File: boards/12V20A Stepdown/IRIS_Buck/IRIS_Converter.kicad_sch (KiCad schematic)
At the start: 27 parts, among them J1 TB005-762-02BE, J2 TB005-762-02BE, Q1 CSD17571Q2, Q2 CSD16340Q3, U1 LM25145RGYR

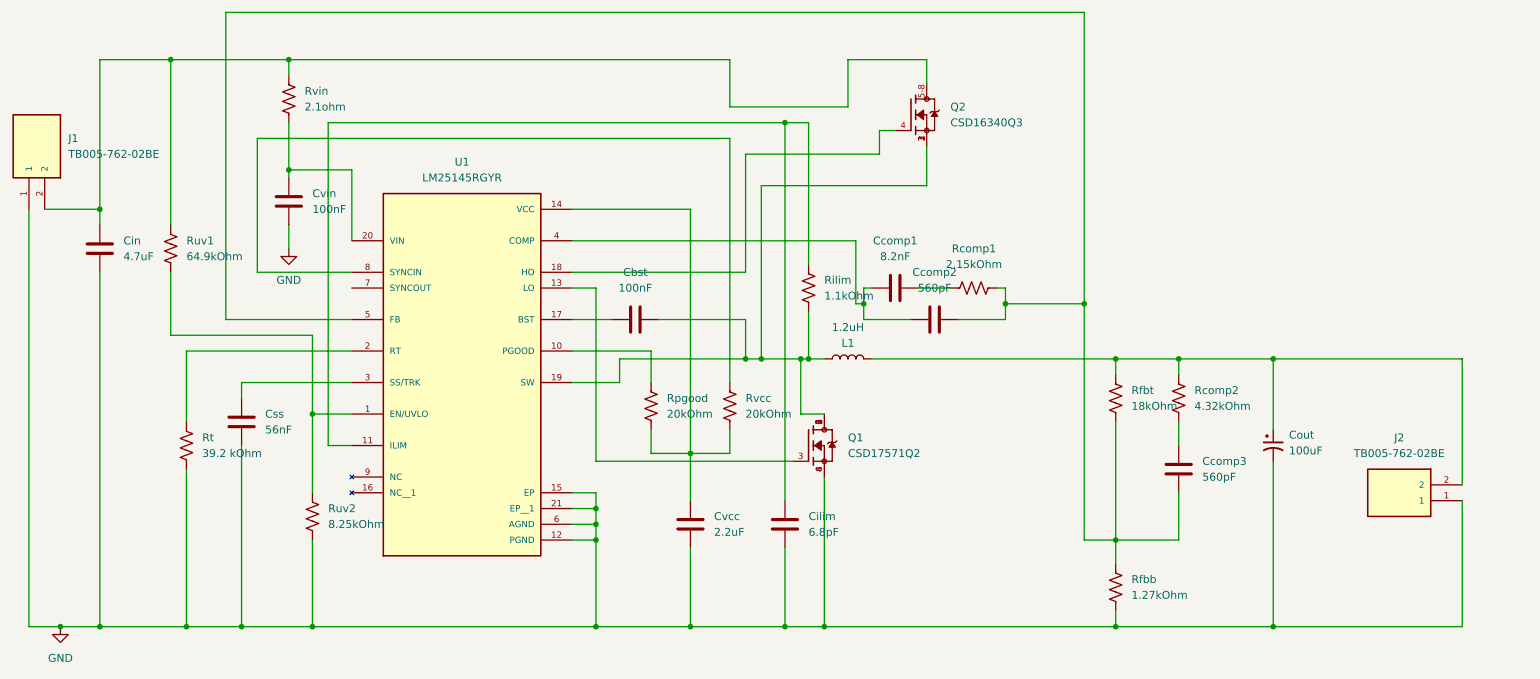
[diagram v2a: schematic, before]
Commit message: Fully updated footprint, start trace
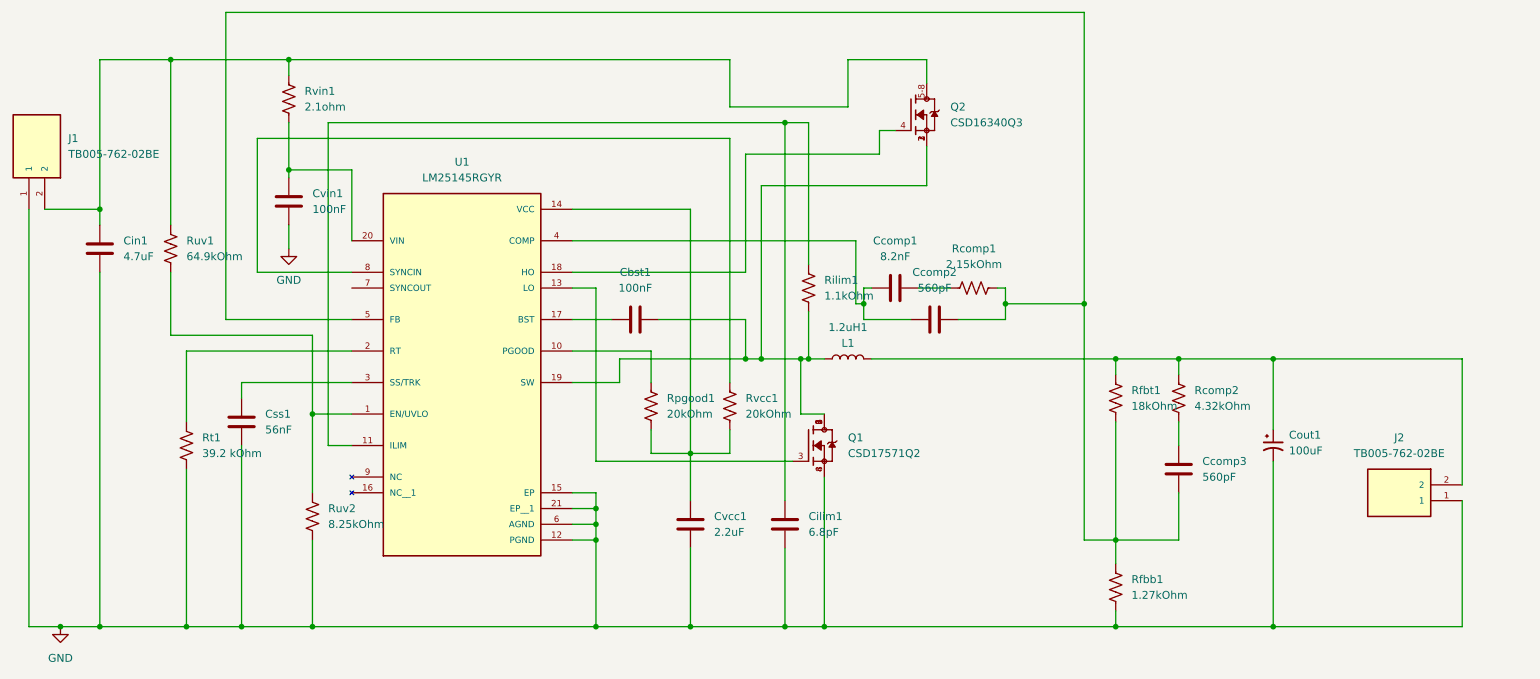
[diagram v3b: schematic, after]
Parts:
- J1, J2: footprint TB005-762-02BE:CUI_TB005-762-02BE -> 10A_LIbrary:TB005-762-02BE_CUD
- Q1: footprint CSD17571Q2:TRANS_CSD17571Q2 -> 20A_Library:DQK0006C
- Q2: footprint CSD16340Q3:TRANS_CSD16340Q3 -> 20A_Library:DQG0008A
- U1: footprint LM25145RGYR:IC_LM25145RGYR -> 20A_Library:RGY0020B
- renumbered 1.2uH to 1.2uH1, Cbst to Cbst1, Cilim to Cilim1, Cin to Cin1, Cout to Cout1, Css to Css1, Cvcc to Cvcc1, Cvin to Cvin1, Rfbb to Rfbb1, Rfbt to Rfbt1, Rilim to Rilim1, Rpgood to Rpgood1, Rt to Rt1, Rvcc to Rvcc1, Rvin to Rvin1
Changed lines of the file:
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@@
 		(dnp no)
 		(fields_autoplaced yes)
-		(property "Reference" "Cilim"
+		(property "Reference" "Cilim1"
 			(at 151.13 129.5399 0)
 			(effects
@@
 			(project "converter"
 				(path "/1513ce43-e5f2-482b-99a2-cdd75b9aa1c1"
-					(reference "Cilim")
+					(reference "Cilim1")
 					(unit 1)
 				)
@@
 			)
 		)
-		(property "Footprint" "CSD16340Q3:TRANS_CSD16340Q3"
+		(property "Footprint" "20A_Library:DQG0008A"
 			(at 167.64 64.77 0)
 			(effects
@@
 			)
 		)
-		(property "Footprint" "LM25145RGYR:IC_LM25145RGYR"
+		(property "Footprint" "20A_Library:RGY0020B"
 			(at 95.25 105.41 0)
 			(effects
@@
 		(dnp no)
 		(fields_autoplaced yes)
-		(property "Reference" "Rfbb"
+		(property "Reference" "Rfbb1"
 			(at 203.2 139.6999 0)
 			(effects
@@
 			(project "converter"
 				(path "/1513ce43-e5f2-482b-99a2-cdd75b9aa1c1"
-					(reference "Rfbb")
+					(reference "Rfbb1")
 					(unit 1)
 				)
@@
 		(dnp no)
 		(fields_autoplaced yes)
-		(property "Reference" "Rt"
+		(property "Reference" "Rt1"
 			(at 53.34 116.8399 0)
 			(effects
@@
 			(project "IRIS_Converter"
 				(path "/1513ce43-e5f2-482b-99a2-cdd75b9aa1c1"
-					(reference "Rt")
+					(reference "Rt1")
 					(unit 1)
 				)
@@
 			)
 		)
-		(property "Footprint" "TB005-762-02BE:CUI_TB005-762-02BE"
+		(property "Footprint" "10A_LIbrary:TB005-762-02BE_CUD"
 			(at 246.38 124.46 0)
 			(effects
@@
 		(dnp no)
 		(fields_autoplaced yes)
-		(property "Reference" "Rpgood"
+		(property "Reference" "Rpgood1"
 			(at 128.27 110.4899 0)
 			(effects
@@
 			(project "converter"
 				(path "/1513ce43-e5f2-482b-99a2-cdd75b9aa1c1"
-					(reference "Rpgood")
+					(reference "Rpgood1")
 					(unit 1)
 				)
@@
 		(dnp no)
 		(fields_autoplaced yes)
-		(property "Reference" "1.2uH"
+		(property "Reference" "1.2uH1"
 			(at 157.48 99.06 90)
 			(effects
@@
 			(project ""
 				(path "/1513ce43-e5f2-482b-99a2-cdd75b9aa1c1"
-					(reference "1.2uH")
+					(reference "1.2uH1")
 					(unit 1)
 				)
@@
 		(dnp no)
 		(fields_autoplaced yes)
-		(property "Reference" "Cin"
+		(property "Reference" "Cin1"
 			(at 40.64 85.0899 0)
 			(effects
@@
 			(project "converter"
 				(path "/1513ce43-e5f2-482b-99a2-cdd75b9aa1c1"
-					(reference "Cin")
+					(reference "Cin1")
 					(unit 1)
 				)
@@
 		(dnp no)
 		(fields_autoplaced yes)
-		(property "Reference" "Cvcc"
+		(property "Reference" "Cvcc1"
 			(at 135.89 129.5399 0)
 			(effects
@@
 			(project ""
 				(path "/1513ce43-e5f2-482b-99a2-cdd75b9aa1c1"
-					(reference "Cvcc")
+					(reference "Cvcc1")
 					(unit 1)
 				)
@@
 		(dnp no)
 		(fields_autoplaced yes)
-		(property "Reference" "Css"
+		(property "Reference" "Css1"
 			(at 63.5 113.0299 0)
 			(effects
@@
 			(project "converter"
 				(path "/1513ce43-e5f2-482b-99a2-cdd75b9aa1c1"
-					(reference "Css")
+					(reference "Css1")
 					(unit 1)
 				)
@@
 		(dnp no)
 		(fields_autoplaced yes)
-		(property "Reference" "Cout"
+		(property "Reference" "Cout1"
 			(at 228.6 116.4081 0)
 			(effects
@@
 			(project ""
 				(path "/1513ce43-e5f2-482b-99a2-cdd75b9aa1c1"
-					(reference "Cout")
+					(reference "Cout1")
 					(unit 1)
 				)
@@
 		(dnp no)
 		(fields_autoplaced yes)
-		(property "Reference" "Rvin"
+		(property "Reference" "Rvin1"
 			(at 69.85 60.9599 0)
 			(effects
@@
 			(project "converter"
 				(path "/1513ce43-e5f2-482b-99a2-cdd75b9aa1c1"
-					(reference "Rvin")
+					(reference "Rvin1")
 					(unit 1)
 				)
@@
 		(dnp no)
 		(fields_autoplaced yes)
-		(property "Reference" "Rvcc"
+		(property "Reference" "Rvcc1"
 			(at 140.97 110.4899 0)
 			(effects
@@
 			(project ""
 				(path "/1513ce43-e5f2-482b-99a2-cdd75b9aa1c1"
-					(reference "Rvcc")
+					(reference "Rvcc1")
 					(unit 1)
 				)
@@
 		(dnp no)
 		(fields_autoplaced yes)
-		(property "Reference" "Cbst"
+		(property "Reference" "Cbst1"
 			(at 123.19 90.17 90)
 			(effects
@@
 			(project "converter"
 				(path "/1513ce43-e5f2-482b-99a2-cdd75b9aa1c1"
-					(reference "Cbst")
+					(reference "Cbst1")
 					(unit 1)
 				)
@@
 			)
 		)
-		(property "Footprint" "CSD17571Q2:TRANS_CSD17571Q2"
+		(property "Footprint" "20A_Library:DQK0006C"
 			(at 151.13 118.11 0)
 			(effects
@@
 			)
 		)
-		(property "Footprint" "TB005-762-02BE:CUI_TB005-762-02BE"
+		(property "Footprint" "10A_LIbrary:TB005-762-02BE_CUD"
 			(at 27.94 69.85 0)
 			(effects
@@
 		(dnp no)
 		(fields_autoplaced yes)
-		(property "Reference" "Rfbt"
+		(property "Reference" "Rfbt1"
 			(at 203.2 109.2199 0)
 			(effects
@@
 			(project "converter"
 				(path "/1513ce43-e5f2-482b-99a2-cdd75b9aa1c1"
-					(reference "Rfbt")
+					(reference "Rfbt1")
 					(unit 1)
 				)
@@
 		(dnp no)
 		(fields_autoplaced yes)
-		(property "Reference" "Cvin"
+		(property "Reference" "Cvin1"
 			(at 71.12 77.4699 0)
 			(effects
@@
 			(project "IRIS_Converter"
 				(path "/1513ce43-e5f2-482b-99a2-cdd75b9aa1c1"
-					(reference "Cvin")
+					(reference "Cvin1")
 					(unit 1)
 				)
@@
 		(on_board no)
 		(dnp no)
-		(property "Reference" "Rilim"
+		(property "Reference" "Rilim1"
 			(at 153.67 91.4399 0)
 			(effects
@@
 			(project "converter"
 				(path "/1513ce43-e5f2-482b-99a2-cdd75b9aa1c1"
-					(reference "Rilim")
-					(unit 1)
-				)
+					(reference "Rilim1")
+					(unit 1)
+				)

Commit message: Finished front and back layout, will check via stitching later
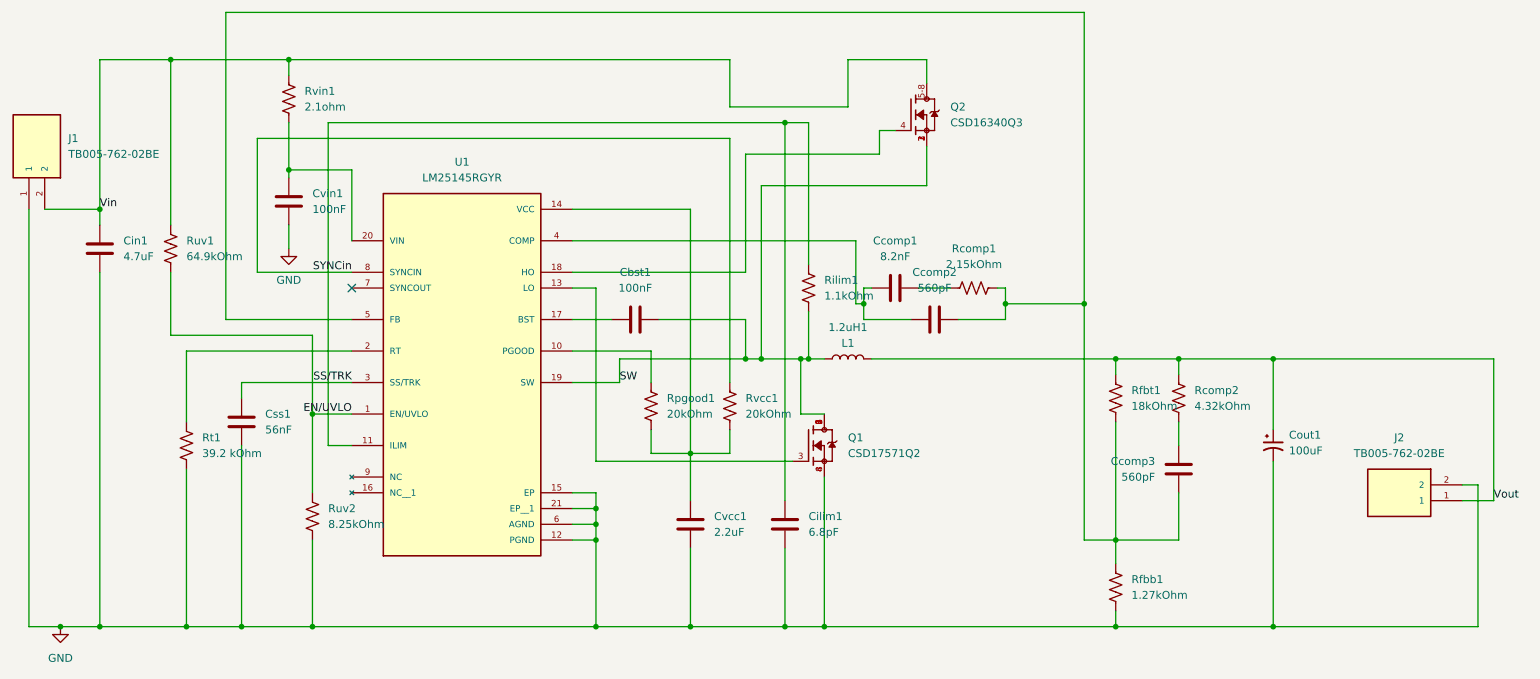
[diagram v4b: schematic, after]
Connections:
- net GND: now also J2.2; no longer J2.1
- net Vin: now reaches Cin1.1, J1.2, Q2.5-8, Ruv1.1, Rvin1.1
- net EN/UVLO: now reaches Ruv1.2, Ruv2.1, U1.1 (EN/UVLO)
- net SW: now reaches 1.2uH1.1, Cbst1.2, Q1.1, Q1.2, Q1.5, Q1.6, Q1.7, Q2.1, Q2.2, Q2.3, Rilim1.2, U1.19 (SW)
- net SS/TRK: now reaches Css1.1, U1.3 (SS/TRK)
- net SYNCin: now reaches Rvcc1.1, U1.8 (SYNCIN)
- net Vout: now reaches 1.2uH1.2, Cout1.1, Rcomp2.1, Rfbt1.1
- net Vout: now also J2.1; no longer J2.2
- no-connect marks 0 -> 1
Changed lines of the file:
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@@
 		(color 0 0 0 0)
 	)
+	(no_connect
+		(at 77.47 92.71)
+	)
 	(wire
 		(pts
@@
 	(wire
 		(pts
-			(xy 149.86 104.14) (xy 151.13 104.14)
+			(xy 259.08 147.32) (xy 259.08 124.46)
 		)
 		(stroke
@@
 	(wire
 		(pts
-			(xy 67.31 55.88) (xy 48.26 55.88)
+			(xy 149.86 104.14) (xy 151.13 104.14)
 		)
 		(stroke
@@
 	(wire
 		(pts
-			(xy 182.88 92.71) (xy 182.88 95.25)
+			(xy 67.31 55.88) (xy 48.26 55.88)
 		)
 		(stroke
@@
 	(wire
 		(pts
-			(xy 175.26 97.79) (xy 182.88 97.79)
+			(xy 182.88 92.71) (xy 182.88 95.25)
 		)
 		(stroke
@@
 	(wire
 		(pts
-			(xy 27.94 80.01) (xy 36.83 80.01)
+			(xy 175.26 97.79) (xy 182.88 97.79)
 		)
 		(stroke
@@
 	(wire
 		(pts
-			(xy 170.18 55.88) (xy 170.18 59.69)
+			(xy 27.94 80.01) (xy 36.83 80.01)
 		)
 		(stroke
@@
 	(wire
 		(pts
-			(xy 140.97 90.17) (xy 140.97 71.12)
+			(xy 170.18 55.88) (xy 170.18 59.69)
 		)
 		(stroke
@@
 	(wire
 		(pts
-			(xy 226.06 104.14) (xy 256.54 104.14)
+			(xy 140.97 90.17) (xy 140.97 71.12)
 		)
 		(stroke
@@
 	(wire
 		(pts
-			(xy 256.54 124.46) (xy 256.54 104.14)
+			(xy 226.06 104.14) (xy 261.62 104.14)
 		)
 		(stroke
@@
 	(wire
 		(pts
+			(xy 261.62 104.14) (xy 261.62 127)
+		)
+		(stroke
+			(width 0)
+			(type default)
+		)
+	)
+	(wire
+		(pts
 			(xy 25.4 147.32) (xy 30.48 147.32)
 		)
@@
 	(wire
 		(pts
+			(xy 256.54 127) (xy 261.62 127)
+		)
+		(stroke
+			(width 0)
+			(type default)
+		)
+	)
+	(wire
+		(pts
 			(xy 168.91 92.71) (xy 173.99 92.71)
 		)
@@
 	(wire
 		(pts
+			(xy 259.08 124.46) (xy 256.54 124.46)
+		)
+		(stroke
+			(width 0)
+			(type default)
+		)
+	)
+	(wire
+		(pts
 			(xy 143.51 76.2) (xy 170.18 76.2)
 		)
@@
 	(wire
 		(pts
-			(xy 256.54 127) (xy 256.54 147.32)
-		)
-		(stroke
-			(width 0)
-			(type default)
-		)
-	)
-	(wire
-		(pts
 			(xy 116.84 147.32) (xy 132.08 147.32)
 		)
@@
 	(wire
 		(pts
-			(xy 256.54 147.32) (xy 226.06 147.32)
+			(xy 226.06 147.32) (xy 259.08 147.32)
 		)
 		(stroke
@@
 		)
 	)
+	(label "EN{slash}UVLO"
+		(at 77.47 113.03 180)
+		(effects
+			(font
+				(size 1.27 1.27)
+			)
+			(justify right bottom)
+		)
+	)
+	(label "SS{slash}TRK"
+		(at 77.47 107.95 180)
+		(effects
+			(font
+				(size 1.27 1.27)
+			)
+			(justify right bottom)
+		)
+	)
+	(label "Vout"
+		(at 261.62 127 0)
+		(effects
+			(font
+				(size 1.27 1.27)
+			)
+			(justify left bottom)
+		)
+	)
+	(label "SW"
+		(at 120.65 107.95 0)
+		(effects
+			(font
+				(size 1.27 1.27)
+			)
+			(justify left bottom)
+		)
+	)
+	(label "Vin"
+		(at 36.83 80.01 0)
+		(effects
+			(font
+				(size 1.27 1.27)
+			)
+			(justify left bottom)
+		)
+	)
+	(label "SYNCin"
+		(at 77.47 90.17 180)
+		(effects
+			(font
+				(size 1.27 1.27)
+			)
+			(justify right bottom)
+		)
+	)
 	(symbol
 		(lib_id "power:GND")
@@
 		(on_board yes)
 		(dnp no)
-		(fields_autoplaced yes)
 		(property "Reference" "Rt1"
 			(at 53.34 116.8399 0)
@@
 		(lib_id "Device:C")
 		(at 210.82 121.92 0)
+		(mirror y)
 		(unit 1)
 		(exclude_from_sim no)
@@
 		(on_board yes)
 		(dnp no)
-		(fields_autoplaced yes)
 		(property "Reference" "Ccomp3"
-			(at 214.63 120.6499 0)
+			(at 207.01 120.6499 0)
 			(effects
 				(font
@@
 		)
 		(property "Value" "560pF"
-			(at 214.63 123.1899 0)
+			(at 207.01 123.1899 0)
 			(effects
 				(font
@@
 		)
 		(property "Footprint" "20A_Library:G-155_MUR"
-			(at 211.7852 125.73 0)
+			(at 209.8548 125.73 0)
 			(effects
 				(font
@@
 		(on_board yes)
 		(dnp no)
-		(fields_autoplaced yes)
 		(property "Reference" "Css1"
 			(at 63.5 113.0299 0)
@@
 		(exclude_from_sim no)
 		(in_bom yes)
-		(on_board no)
+		(on_board yes)
 		(dnp no)
 		(property "Reference" "Rilim1"

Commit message: Added mounting holes and generated manu files
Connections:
- net GND: now also J1.2, J2.1; no longer J1.1, J2.2
- net Vin: now also J1.1; no longer J1.2
- net Vout: now also J2.2; no longer J2.1
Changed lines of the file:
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@@
-	)
-	(junction
-		(at 36.83 80.01)
-		(diameter 0)
-		(color 0 0 0 0)
 	)
 	(junction
@@
 	(junction
 		(at 48.26 55.88)
+		(diameter 0)
+		(color 0 0 0 0)
+	)
+	(junction
+		(at 36.83 82.55)
 		(diameter 0)
 		(color 0 0 0 0)
@@
 	(wire
 		(pts
-			(xy 36.83 55.88) (xy 36.83 80.01)
+			(xy 36.83 55.88) (xy 36.83 82.55)
 		)
 		(stroke
@@
 	(wire
 		(pts
-			(xy 259.08 147.32) (xy 259.08 124.46)
+			(xy 259.08 149.86) (xy 259.08 127)
 		)
 		(stroke
@@
 	(wire
 		(pts
-			(xy 27.94 80.01) (xy 36.83 80.01)
-		)
-		(stroke
-			(width 0)
-			(type default)
-		)
-	)
-	(wire
-		(pts
 			(xy 170.18 55.88) (xy 170.18 59.69)
 		)
@@
 	(wire
 		(pts
+			(xy 27.94 87.63) (xy 27.94 80.01)
+		)
+		(stroke
+			(width 0)
+			(type default)
+		)
+	)
+	(wire
+		(pts
 			(xy 226.06 104.14) (xy 261.62 104.14)
 		)
@@
 	(wire
 		(pts
+			(xy 25.4 87.63) (xy 27.94 87.63)
+		)
+		(stroke
+			(width 0)
+			(type default)
+		)
+	)
+	(wire
+		(pts
 			(xy 73.66 66.04) (xy 147.32 66.04)
 		)
@@
 	(wire
 		(pts
-			(xy 261.62 104.14) (xy 261.62 127)
+			(xy 261.62 104.14) (xy 261.62 124.46)
 		)
 		(stroke
@@
 	(wire
 		(pts
-			(xy 256.54 127) (xy 261.62 127)
+			(xy 25.4 147.32) (xy 25.4 87.63)
 		)
 		(stroke
@@
 	(wire
 		(pts
+			(xy 25.4 80.01) (xy 25.4 82.55)
+		)
+		(stroke
+			(width 0)
+			(type default)
+		)
+	)
+	(wire
+		(pts
 			(xy 67.31 66.04) (xy 67.31 73.66)
 		)
@@
 	(wire
 		(pts
+			(xy 226.06 149.86) (xy 226.06 147.32)
+		)
+		(stroke
+			(width 0)
+			(type default)
+		)
+	)
+	(wire
+		(pts
 			(xy 62.23 68.58) (xy 62.23 90.17)
 		)
@@
 	(wire
 		(pts
-			(xy 36.83 80.01) (xy 36.83 82.55)
-		)
-		(stroke
-			(width 0)
-			(type default)
-		)
-	)
-	(wire
-		(pts
 			(xy 113.03 102.87) (xy 125.73 102.87)
 		)
@@
 	(wire
 		(pts
+			(xy 256.54 127) (xy 259.08 127)
+		)
+		(stroke
+			(width 0)
+			(type default)
+		)
+	)
+	(wire
+		(pts
 			(xy 160.02 95.25) (xy 160.02 97.79)
 		)
@@
 	(wire
 		(pts
-			(xy 259.08 124.46) (xy 256.54 124.46)
-		)
-		(stroke
-			(width 0)
-			(type default)
-		)
-	)
-	(wire
-		(pts
 			(xy 143.51 76.2) (xy 170.18 76.2)
 		)
@@
 	(wire
 		(pts
+			(xy 256.54 124.46) (xy 261.62 124.46)
+		)
+		(stroke
+			(width 0)
+			(type default)
+		)
+	)
+	(wire
+		(pts
 			(xy 71.12 100.33) (xy 71.12 113.03)
 		)
@@
 	(wire
 		(pts
-			(xy 226.06 147.32) (xy 259.08 147.32)
-		)
-		(stroke
-			(width 0)
-			(type default)
-		)
-	)
-	(wire
-		(pts
-			(xy 25.4 80.01) (xy 25.4 147.32)
+			(xy 226.06 149.86) (xy 259.08 149.86)
 		)
 		(stroke
@@
 		(pts
 			(xy 57.15 97.79) (xy 57.15 48.26)
+		)
+		(stroke
+			(width 0)
+			(type default)
+		)
+	)
+	(wire
+		(pts
+			(xy 25.4 82.55) (xy 36.83 82.55)
 		)
 		(stroke
@@
 	)
 	(label "Vout"
-		(at 261.62 127 0)
+		(at 261.62 124.46 0)
 		(effects
 			(font
